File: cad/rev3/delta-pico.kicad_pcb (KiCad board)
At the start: 2 copper layers, 77.7 x 166.3 mm, 76 parts, among them J1 Conn_01x02, J2 Conn_01x14, J3 Conn_01x08, J4 Conn_01x04, J5 Conn_01x03, SW1 SW_SPDT, SW10 SW_Push, SW11 SW_Push, SW12 SW_Push, SW13 SW_Push, SW14 SW_Push, SW15 SW_Push, SW16 SW_Push, SW17 SW_Push, SW18 SW_Push, SW19 SW_Push, SW2 SW_Push, SW20 SW_Push, SW21 SW_Push, SW22 SW_Push, SW23 SW_Push, SW24 SW_Push, SW25 SW_Push, SW26 SW_Push, SW27 SW_Push, SW28 SW_Push, SW29 SW_Push, SW3 SW_Push, SW30 SW_Push, SW31 SW_Push, SW4 SW_Push, SW5 SW_Push, SW6 SW_Push, SW7 SW_Push, SW8 SW_Push, SW9 SW_Push, U1 PCF8574A, U2 PCF8574A, U3 Pico, U4 24LC16

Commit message: Pico calls it VSYS, not VIN
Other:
- board text added: "BYP. VSYS"
- board text added: "SW. VSYS"
- board text removed: "BYP. VIN"
- board text removed: "SW. VIN"
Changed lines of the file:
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@@
     (effects (font (size 1 1) (thickness 0.15)) (justify mirror))
   )
-  (gr_text "BYP. VIN" (at 59.660333 27.960333 90) (layer "B.SilkS")
+  (gr_text "BYP. VSYS" (at 59.65 28.53 90) (layer "B.SilkS")
     (effects (font (size 0.8 0.8) (thickness 0.15)) (justify mirror))
   )
-  (gr_text "SW. VIN" (at 57.010333 27.580333 90) (layer "B.SilkS")
+  (gr_text "SW. VSYS" (at 56.98 28.23 90) (layer "B.SilkS")
     (effects (font (size 0.8 0.8) (thickness 0.15)) (justify mirror))
   )

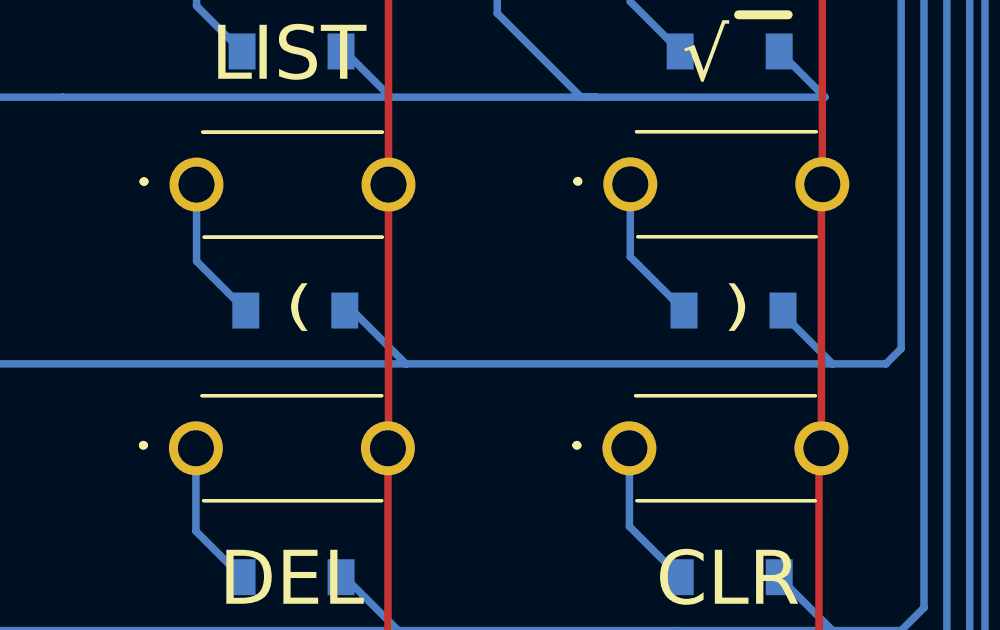
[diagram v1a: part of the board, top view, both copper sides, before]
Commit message: Merge bracket keys, add "TEXT" key
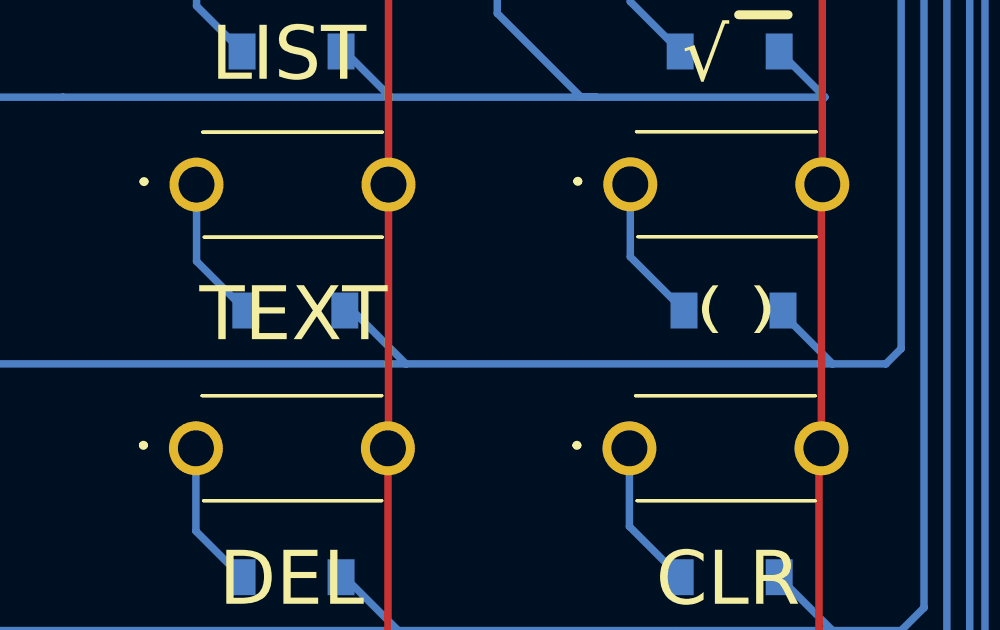
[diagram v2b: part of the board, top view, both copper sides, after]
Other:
- board text added: "( )"
- board text added: "TEXT"
- board text removed: "("
- board text removed: ")"
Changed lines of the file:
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@@
     (effects (font (size 1.8 1.8) (thickness 0.3)))
   )
-  (gr_text "(" (at 86.800333 140.550333) (layer "F.SilkS")
-    (effects (font (size 1.3 1.8) (thickness 0.3)))
-  )
-  (gr_text ")" (at 101.400333 140.550333) (layer "F.SilkS")
+  (gr_text "( )" (at 101.37 140.62) (layer "F.SilkS")
     (effects (font (size 1.3 1.8) (thickness 0.3)))
   )
@@
     (effects (font (size 7.5 13.35) (thickness 0.9)))
   )
+  (gr_text "TEXT" (at 86.61 140.83) (layer "F.SilkS")
+    (effects (font (size 1.8 1.8) (thickness 0.3)))
+  )
   (dimension (type aligned) (layer "Dwgs.User")

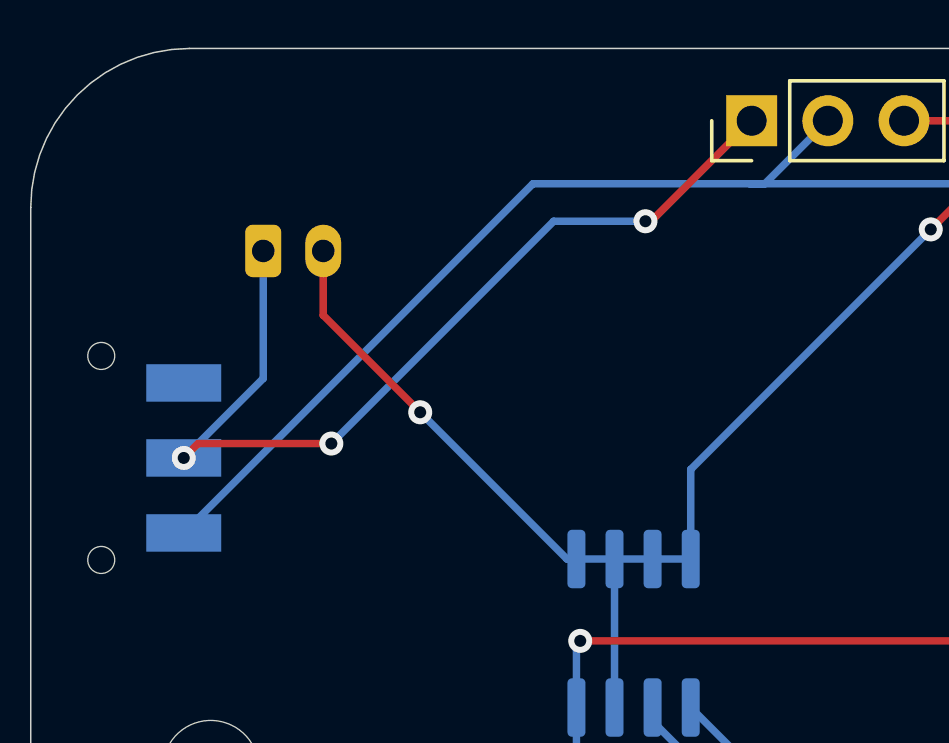
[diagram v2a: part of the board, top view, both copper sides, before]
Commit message: Add Schottky diode on VSYS
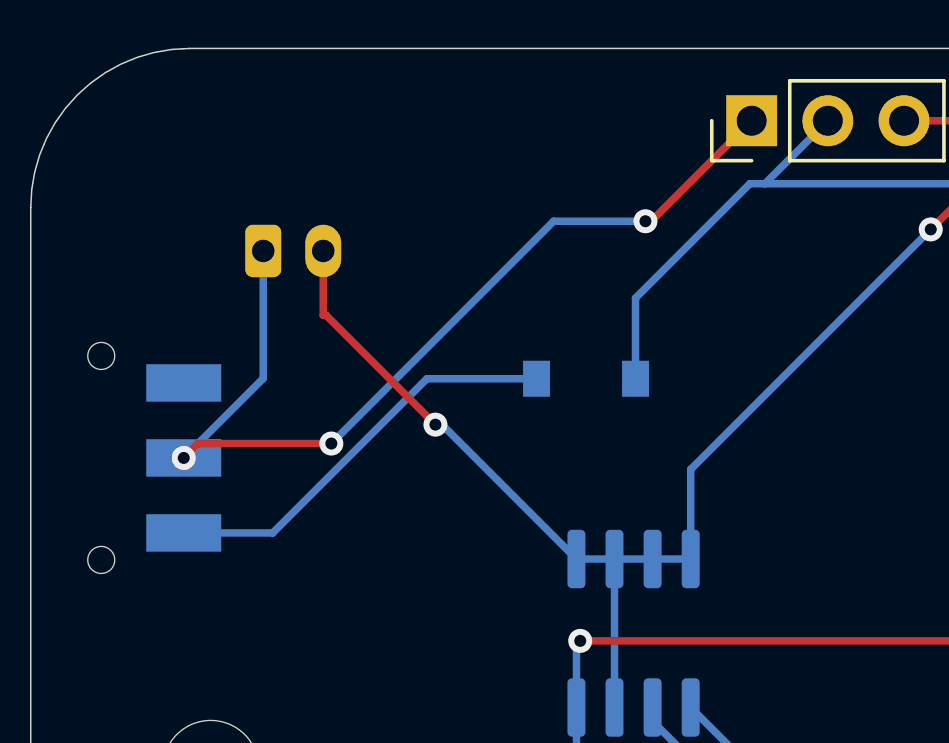
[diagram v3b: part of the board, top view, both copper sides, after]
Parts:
- added D31: D_Schottky, Diode_SMD:D_SOD-123, B.Cu at (51.5, 32.0)
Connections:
- SW1 pad 1: VIN -> Net-(SW1-Pad1)
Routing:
- net VIN: track 51.8 -> 35.6 mm
- net Net-(SW1-Pad1): track 0.00 -> 13.9 mm
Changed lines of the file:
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@@
   (net 95 "COLINT")
   (net 96 "ROWINT")
+  (net 97 "Net-(SW1-Pad1)")
   (footprint "PTS636SL43LFS:PTS636SL43LFS" (layer "F.Cu")
     (at 43.622333 133.596333 90)
@@
     (pad "" np_thru_hole circle locked (at -3.4 0 90) (size 0.9 0.9) (drill 0.9) (layers *.Cu *.Mask))
     (pad "1" smd rect locked (at -2.5 2.75 90) (size 1.25 2.5) (layers "B.Cu" "B.Paste" "B.Mask")
-      (net 52 "VIN") (pinfunction "A") (pintype "passive"))
+      (net 97 "Net-(SW1-Pad1)") (pinfunction "A") (pintype "passive"))
     (pad "2" smd rect locked (at 0 2.75 90) (size 1.25 2.5) (layers "B.Cu" "B.Paste" "B.Mask")
       (net 38 "RAWVIN") (pinfunction "B") (pintype "passive"))
@@
     )
   )
+  (footprint "Diode_SMD:D_SOD-123" (layer "B.Cu")
+    (at 51.51 32.01 180)
+    (descr "SOD-123")
+    (tags "SOD-123")
+    (property "Sheetfile" "delta-pico.kicad_sch")
+    (property "Sheetname" "")
+    (attr smd)
+    (fp_text reference "D31" (at 0 2) (layer "B.SilkS") hide
+      (effects (font (size 1 1) (thickness 0.15)) (justify mirror))
+    )
+    (fp_text value "D_Schottky" (at 0 -2.1) (layer "B.Fab")
+      (effects (font (size 1 1) (thickness 0.15)) (justify mirror))
+    )
+    (fp_text user "${REFERENCE}" (at 0 2) (layer "B.Fab")
+      (effects (font (size 1 1) (thickness 0.15)) (justify mirror))
+    )
+    (fp_line (start -2.25 -1) (end 1.65 -1) (layer "B.SilkS") (width 0.12))
+    (fp_line (start -2.25 1) (end 1.65 1) (layer "B.SilkS") (width 0.12))
+    (fp_line (start -2.25 1) (end -2.25 -1) (layer "B.SilkS") (width 0.12))
+    (fp_line (start -2.35 1.15) (end -2.35 -1.15) (layer "B.CrtYd") (width 0.05))
+    (fp_line (start 2.35 -1.15) (end -2.35 -1.15) (layer "B.CrtYd") (width 0.05))
+    (fp_line (start -2.35 1.15) (end 2.35 1.15) (layer "B.CrtYd") (width 0.05))
+    (fp_line (start 2.35 1.15) (end 2.35 -1.15) (layer "B.CrtYd") (width 0.05))
+    (fp_line (start -0.35 0) (end 0.25 0.4) (layer "B.Fab") (width 0.1))
+    (fp_line (start 0.25 -0.4) (end -0.35 0) (layer "B.Fab") (width 0.1))
+    (fp_line (start 1.4 -0.9) (end -1.4 -0.9) (layer "B.Fab") (width 0.1))
+    (fp_line (start 1.4 0.9) (end 1.4 -0.9) (layer "B.Fab") (width 0.1))
+    (fp_line (start 0.25 0.4) (end 0.25 -0.4) (layer "B.Fab") (width 0.1))
+    (fp_line (start -1.4 -0.9) (end -1.4 0.9) (layer "B.Fab") (width 0.1))
+    (fp_line (start -1.4 0.9) (end 1.4 0.9) (layer "B.Fab") (width 0.1))
+    (fp_line (start -0.35 0) (end -0.35 -0.55) (layer "B.Fab") (width 0.1))
+    (fp_line (start -0.35 0) (end -0.35 0.55) (layer "B.Fab") (width 0.1))
+    (fp_line (start -0.75 0) (end -0.35 0) (layer "B.Fab") (width 0.1))
+    (fp_line (start 0.25 0) (end 0.75 0) (layer "B.Fab") (width 0.1))
+    (pad "1" smd rect locked (at -1.65 0 180) (size 0.9 1.2) (layers "B.Cu" "B.Paste" "B.Mask")
+      (net 52 "VIN") (pinfunction "K") (pintype "passive"))
+    (pad "2" smd rect locked (at 1.65 0 180) (size 0.9 1.2) (layers "B.Cu" "B.Paste" "B.Mask")
+      (net 97 "Net-(SW1-Pad1)") (pinfunction "A") (pintype "passive"))
+    (model "${KICAD6_3DMODEL_DIR}/Diode_SMD.3dshapes/D_SOD-123.wrl"
+      (offset (xyz 0 0 0))
+      (scale (xyz 1 1 1))
+      (rotate (xyz 0 0 0))
+    )
+  )
+  (gr_line (start 51.62 29.32) (end 51.62 29.16) (layer "B.SilkS") (width 0.12))
+  (gr_line (start 51.93 30.65) (end 52.21 30.65) (layer "B.SilkS") (width 0.12))
+  (gr_line (start 50.78 29.18) (end 50.78 30.62) (layer "B.SilkS") (width 0.12))
+  (gr_line (start 50.78 30.62) (end 51.93 29.88) (layer "B.SilkS") (width 0.12))
+  (gr_line (start 51.93 30.64) (end 51.93 29.17) (layer "B.SilkS") (width 0.12))
+  (gr_line (start 52.21 30.65) (end 52.21 30.49) (layer "B.SilkS") (width 0.12))
+  (gr_line (start 51.64 29.16) (end 51.93 29.16) (layer "B.SilkS") (width 0.12))
+  (gr_line (start 51.93 29.88) (end 50.78 29.18) (layer "B.SilkS") (width 0.12))
   (gr_poly
     (pts
@@
   (segment (start 60.400333 111.100333) (end 57.640333 108.340333) (width 0.25) (layer "F.Cu") (net 37))
   (segment (start 48.205333 98.065333) (end 40.575333 98.065333) (width 0.25) (layer "F.Cu") (net 37))
+  (segment (start 42.750333 29.896333) (end 42.846333 29.896333) (width 0.25) (layer "F.Cu") (net 37))
   (segment (start 67.366333 22.666333) (end 68.334333 21.698333) (width 0.25) (layer "F.Cu") (net 37))
+  (segment (start 42.846333 29.896333) (end 46.49 33.54) (width 0.25) (layer "F.Cu") (net 37))
   (segment (start 63.000333 27.032333) (end 67.366333 22.666333) (width 0.25) (layer "F.Cu") (net 37))
   (segment (start 42.750333 29.896333) (end 42.750333 27.750333) (width 0.25) (layer "F.Cu") (net 37))
-  (segment (start 45.982333 33.128333) (end 42.750333 29.896333) (width 0.25) (layer "F.Cu") (net 37))
   (segment (start 107.050333 37.250333) (end 107.050333 37.200333) (width 0.25) (layer "F.Cu") (net 37))
   (segment (start 57.640333 108.340333) (end 57.640333 107.500333) (width 0.25) (layer "F.Cu") (net 37))
@@
   (via (at 107.050333 37.200333) (size 0.8) (drill 0.4) (layers "F.Cu" "B.Cu") (net 37))
   (via (at 103.538733 27.946733) (size 0.8) (drill 0.4) (layers "F.Cu" "B.Cu") (net 37))
-  (via (at 45.982333 33.128333) (size 0.8) (drill 0.4) (layers "F.Cu" "B.Cu") (net 37))
+  (via (at 46.49 33.54) (size 0.8) (drill 0.4) (layers "F.Cu" "B.Cu") (net 37))
   (segment (start 107.050333 28.969133) (end 106.027933 27.946733) (width 0.25) (layer "B.Cu") (net 37))
   (segment (start 86.675333 112.690333) (end 93.510333 112.690333) (width 0.25) (layer "B.Cu") (net 37))
   (segment (start 61.990333 112.690333) (end 60.400333 111.100333) (width 0.25) (layer "B.Cu") (net 37))
   (segment (start 93.510333 112.690333) (end 109.550333 96.650333) (width 0.25) (layer "B.Cu") (net 37))
+  (segment (start 46.49 33.54) (end 46.71 33.54) (width 0.25) (layer "B.Cu") (net 37))
   (segment (start 54.999333 38.019333) (end 54.999333 35.033333) (width 0.25) (layer "B.Cu") (net 37))
   (segment (start 86.675333 112.690333) (end 86.675333 111.665333) (width 0.25) (layer "B.Cu") (net 37))
   (segment (start 54.999333 35.033333) (end 63.000333 27.032333) (width 0.25) (layer "B.Cu") (net 37))
   (segment (start 62.830333 112.690333) (end 61.990333 112.690333) (width 0.25) (layer "B.Cu") (net 37))
+  (segment (start 46.71 33.54) (end 51.189333 38.019333) (width 0.25) (layer "B.Cu") (net 37))
   (segment (start 52.459333 42.969333) (end 52.459333 38.019333) (width 0.25) (layer "B.Cu") (net 37))
-  (segment (start 50.873333 38.019333) (end 45.982333 33.128333) (width 0.25) (layer "B.Cu") (net 37))
-  (segment (start 51.189333 38.019333) (end 50.873333 38.019333) (width 0.25) (layer "B.Cu") (net 37))
   (segment (start 52.459333 38.019333) (end 51.189333 38.019333) (width 0.25) (layer "B.Cu") (net 37))
   (segment (start 66.609333 112.690333) (end 65.339333 112.690333) (width 0.25) (layer "B.Cu") (net 37))
@@
   (segment (start 103.250333 75.199733) (end 103.729233 74.720833) (width 0.25) (layer "B.Cu") (net 50))
   (segment (start 81.413333 25.510333) (end 81.516933 25.406733) (width 0.25) (layer "B.Cu") (net 52))
-  (segment (start 49.740333 25.510333) (end 56.970333 25.510333) (width 0.25) (layer "B.Cu") (net 52))
   (segment (start 56.970333 25.510333) (end 81.413333 25.510333) (width 0.25) (layer "B.Cu") (net 52))
-  (segment (start 38.100333 37.150333) (end 49.740333 25.510333) (width 0.25) (layer "B.Cu") (net 52))
-  (segment (start 57.470333 25.510333) (end 56.970333 25.510333) (width 0.25) (layer "B.Cu") (net 52))
+  (segment (start 53.16 29.320666) (end 56.970333 25.510333) (width 0.25) (layer "B.Cu") (net 52))
+  (segment (start 53.16 32.01) (end 53.16 29.320666) (width 0.25) (layer "B.Cu") (net 52))
   (segment (start 59.570333 23.410333) (end 57.470333 25.510333) (width 0.25) (layer "B.Cu") (net 52))
   (segment (start 46.360333 162.710333) (end 46.360333 154.040333) (width 0.25) (layer "F.Cu") (net 53))
@@
   (segment (start 74.390333 69.260333) (end 75.063933 68.586733) (width 0.25) (layer "B.Cu") (net 96))
   (segment (start 75.063933 68.586733) (end 81.516933 68.586733) (width 0.25) (layer "B.Cu") (net 96))
+  (segment (start 38.100333 37.150333) (end 41.064947 37.150333) (width 0.25) (layer "B.Cu") (net 97))
+  (segment (start 46.20528 32.01) (end 49.86 32.01) (width 0.25) (layer "B.Cu") (net 97))
+  (segment (start 41.064947 37.150333) (end 46.20528 32.01) (width 0.25) (layer "B.Cu") (net 97))
   (zone (net 0) (net_name "") (layer "B.Cu") (hatch edge 0.508)
     (connect_pads (clearance 0))

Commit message: Add MOSFET for display power control
And if that doesn't work, there's a jumper to bypass it
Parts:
- added JP1: SolderJumper_2_Open, Jumper:SolderJumper-2_P1.3mm_Open_RoundedPad1.0x1.5mm, B.Cu at (63.2, 102.9)
- added Q1: 2N7002K, Package_TO_SOT_SMD:SOT-23, B.Cu at (59.9, 102.9)
- added R1: 10k, Resistor_SMD:R_0603_1608Metric_Pad0.98x0.95mm_HandSolder, B.Cu at (59.9, 99.6)
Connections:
- J2 pad 2: GND -> DISPLAY_GND
- U3 pad 29: unconnected-(U3-Pad29) -> DISPLAY_GATE
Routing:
- net DISPLAY_GATE: track 0.00 -> 70.6 mm, vias 0 -> 2
- net GND: track 253.5 -> 269.5 mm
- net DISPLAY_GND: track 0.00 -> 8.09 mm

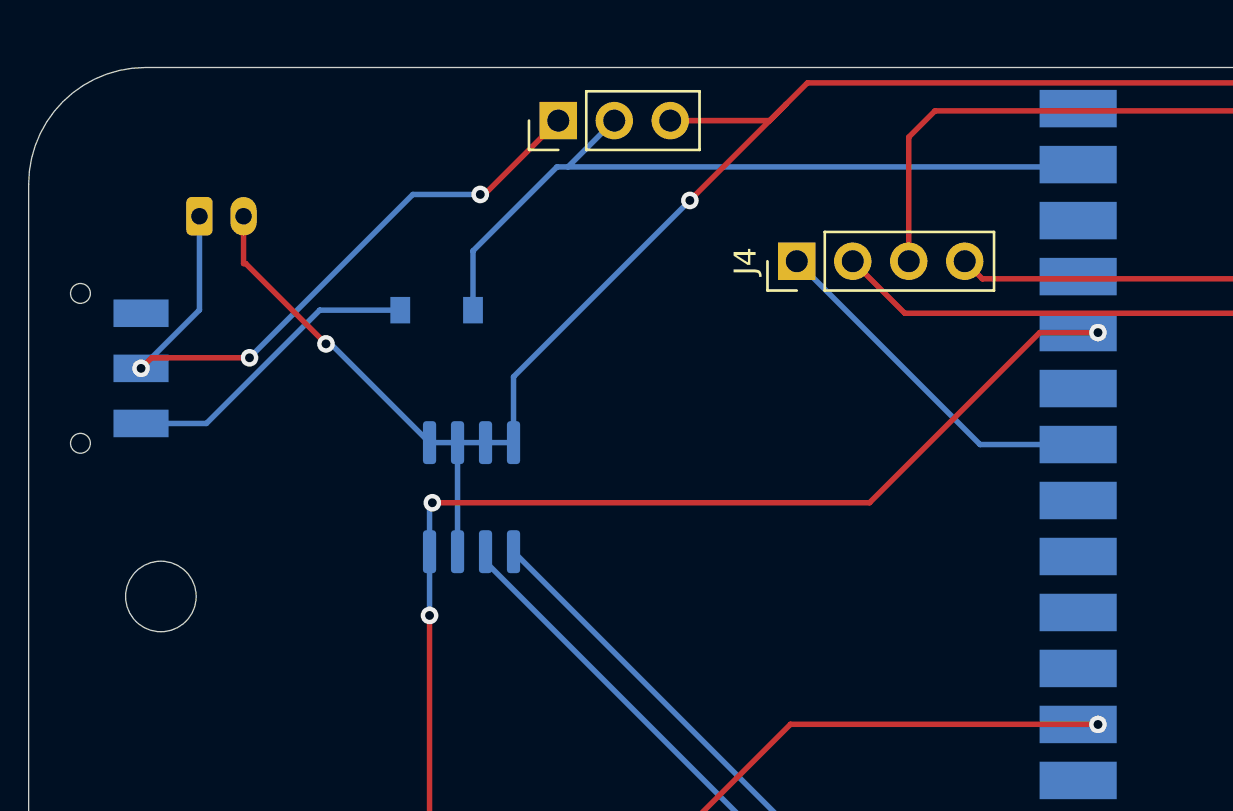
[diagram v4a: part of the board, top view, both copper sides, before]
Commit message: Make power switch soft
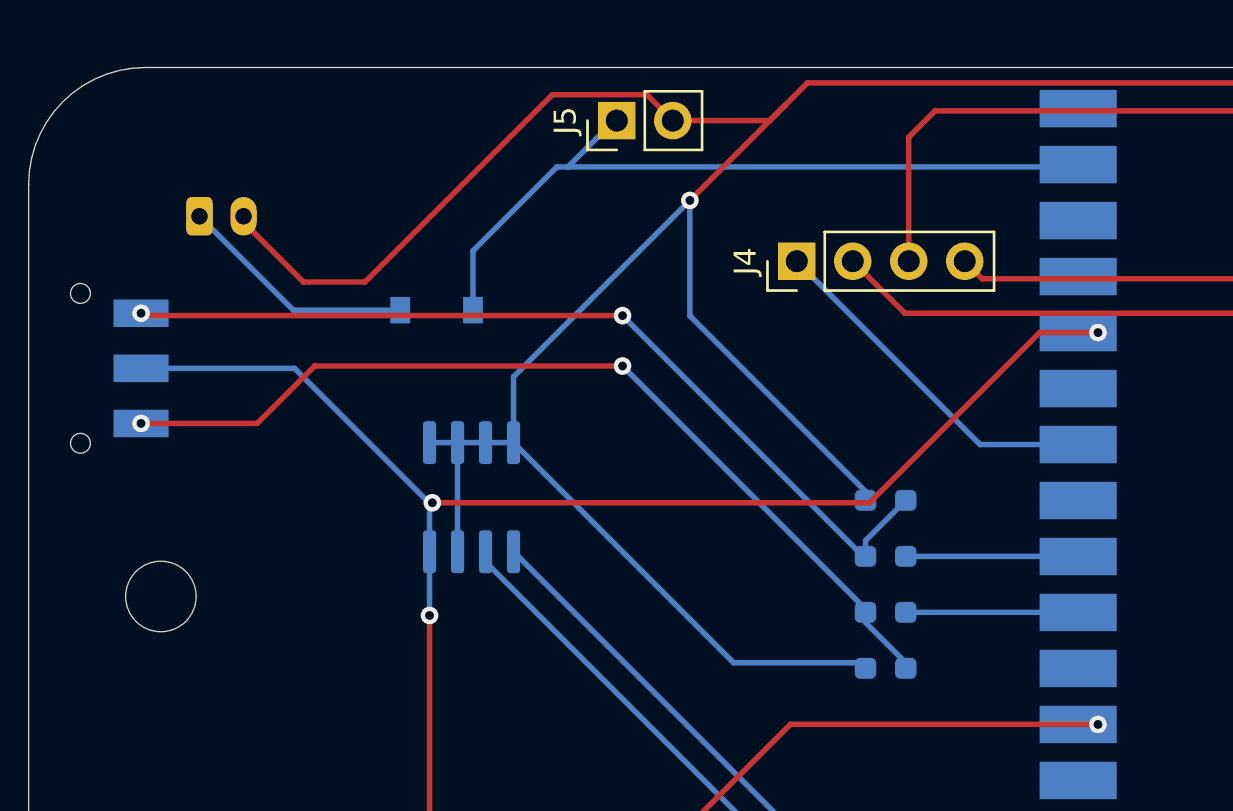
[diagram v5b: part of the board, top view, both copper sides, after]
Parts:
- added R2: 10k, Resistor_SMD:R_0603_1608Metric_Pad0.98x0.95mm_HandSolder, B.Cu at (71.9, 40.6)
- added R3: 10k, Resistor_SMD:R_0603_1608Metric_Pad0.98x0.95mm_HandSolder, B.Cu at (71.9, 48.3)
- added R4: 10k, Resistor_SMD:R_0603_1608Metric_Pad0.98x0.95mm_HandSolder, B.Cu at (71.9, 43.2)
- added R5: 10k, Resistor_SMD:R_0603_1608Metric_Pad0.98x0.95mm_HandSolder, B.Cu at (71.9, 45.7)
- J5: value Conn_01x03 -> Conn_01x02; footprint Connector_PinHeader_2.54mm:PinHeader_1x03_P2.54mm_Vertical -> Connector_PinHeader_2.54mm:PinHeader_1x02_P2.54mm_Vertical
- moved J5 2.65 mm to (59.7, 23.4)
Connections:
- D31 pad 2: Net-(D31-Pad2) -> Net-(J1-Pad1)
- J1 pad 1: RAWVIN -> Net-(J1-Pad1)
- J5 pad 1: RAWVIN -> VIN
- J5 pad 2: VIN -> GND
- SW1 pad 1: Net-(D31-Pad2) -> Net-(SW1-Pad1)
- SW1 pad 2: RAWVIN -> 3V3
- SW1 pad 3: unconnected-(SW1-Pad3) -> Net-(SW1-Pad3)
- U3 pad 31: unconnected-(U3-Pad31) -> POWER_ON
- U3 pad 32: unconnected-(U3-Pad32) -> POWER_OFF
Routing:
- net GND: track 269.5 -> 317.5 mm, vias 6 -> 5
- net Net-(SW1-Pad1): track 0.00 -> 41.7 mm, vias 0 -> 2
- net Net-(SW1-Pad3): track 0.00 -> 40.7 mm, vias 0 -> 2
- net RAWVIN: track 31.6 -> 0.00 mm, vias 3 -> 0
- net 3V3: track 173.2 -> 189.0 mm
- net Net-(D31-Pad2): track 13.9 -> 0.00 mm
- net Net-(J1-Pad1): track 0.00 -> 10.9 mm
- net POWER_ON: track 0.00 -> 8.73 mm
- net POWER_OFF: track 0.00 -> 8.73 mm
